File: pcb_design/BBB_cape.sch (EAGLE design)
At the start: 4 parts

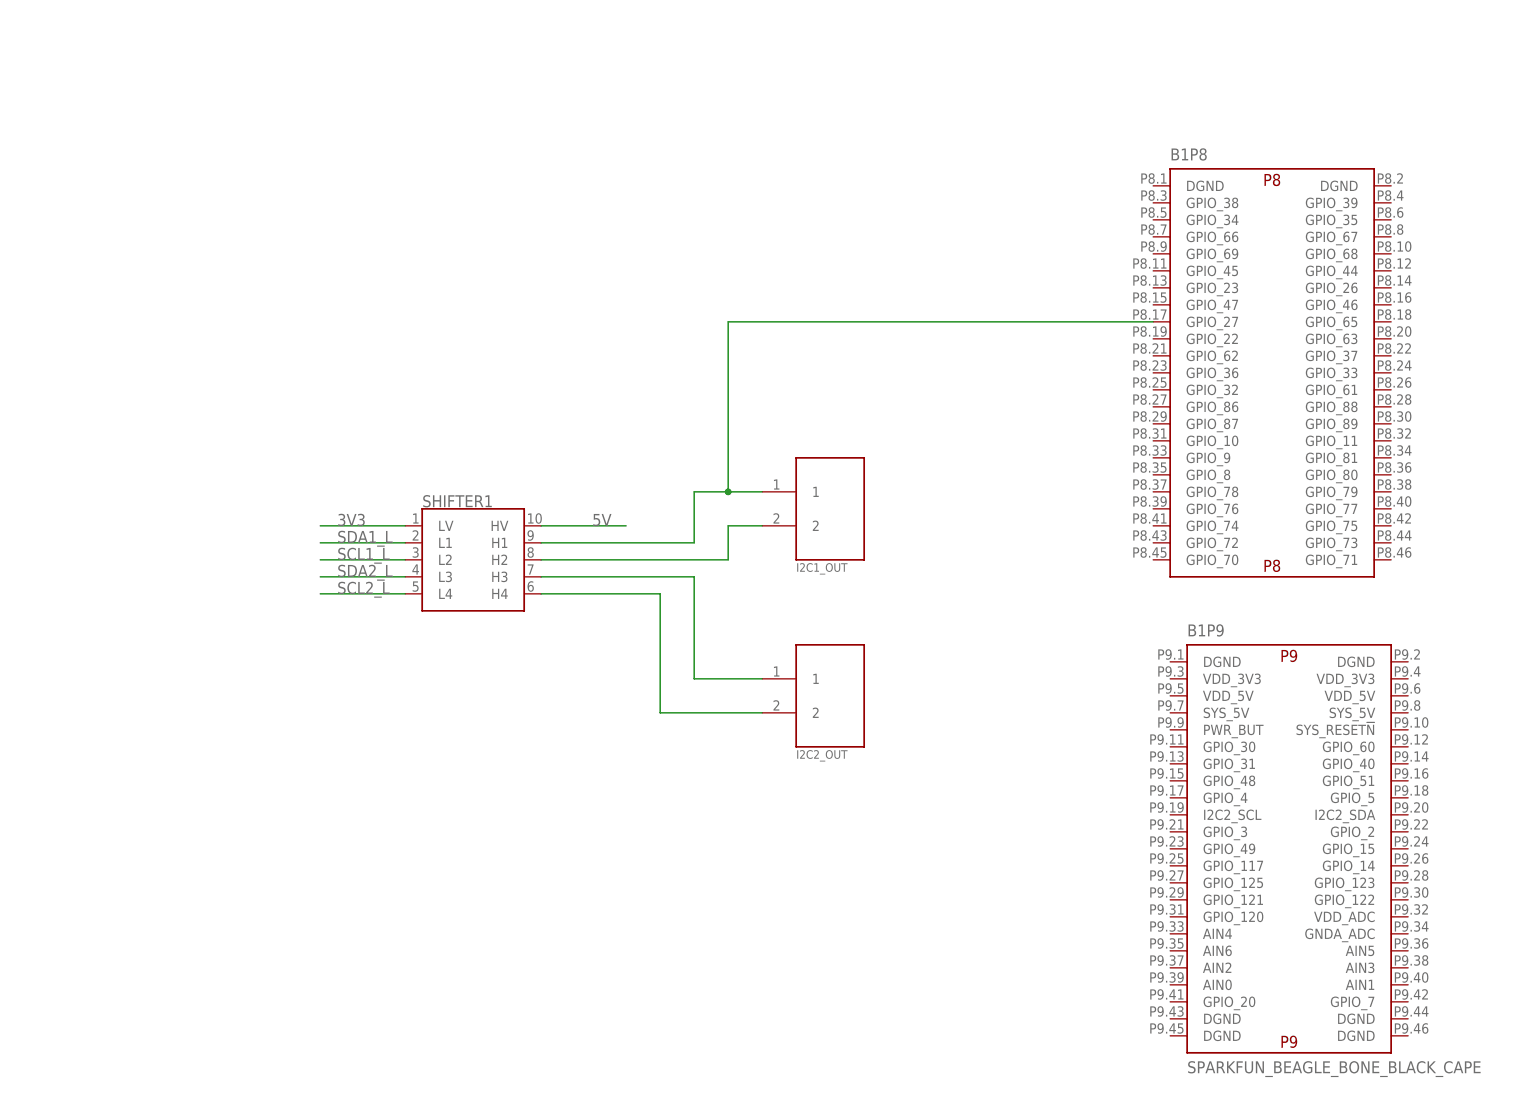
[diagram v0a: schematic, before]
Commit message: added v6 with better connectors and some small drill changes
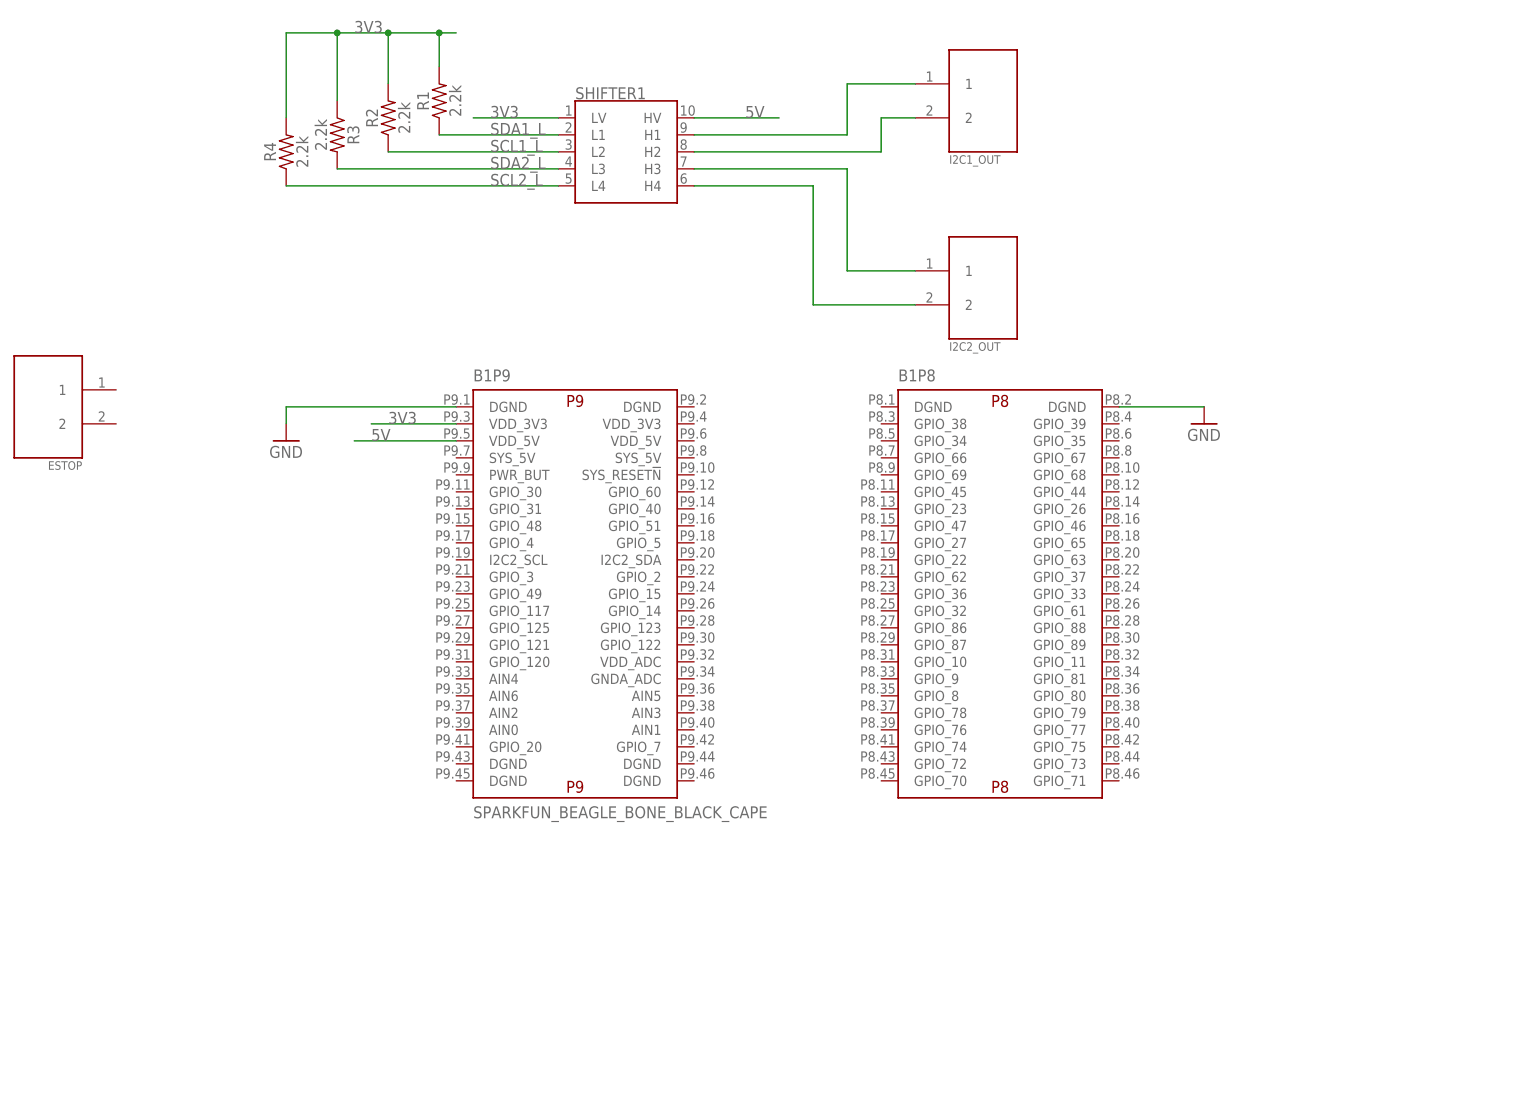
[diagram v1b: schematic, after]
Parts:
- added ESTOP: PHOENIX_CONNECTOR_1778625, byu_pressure_control:PHOENIX_CONNECTOR_1778625
- added R1, R2, R3, R4: 2.2k, SparkFun-Resistors:1KOHM-HORIZ_KIT-1/4W-5%
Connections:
- new net GND: B1P8.DGND@2, B1P9.DGND@1
- net 3V3: now also B1P9.VDD_3V3@1, R1.2, R2.2, R3.1, R4.2
- net 5V: now also B1P9.VDD_5V@1
- net N$1: no longer B1P8.GPIO_27
- net SCL1_L: now also R2.1
- net SCL2_L: now also R4.1
- net SDA1_L: now also R1.1
- net SDA2_L: now also R3.2
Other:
- moved on the sheet: B1P8, B1P9, I2C1_OUT, I2C2_OUT, SHIFTER1

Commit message: removed old files and updated with CAM files for both pcbs.
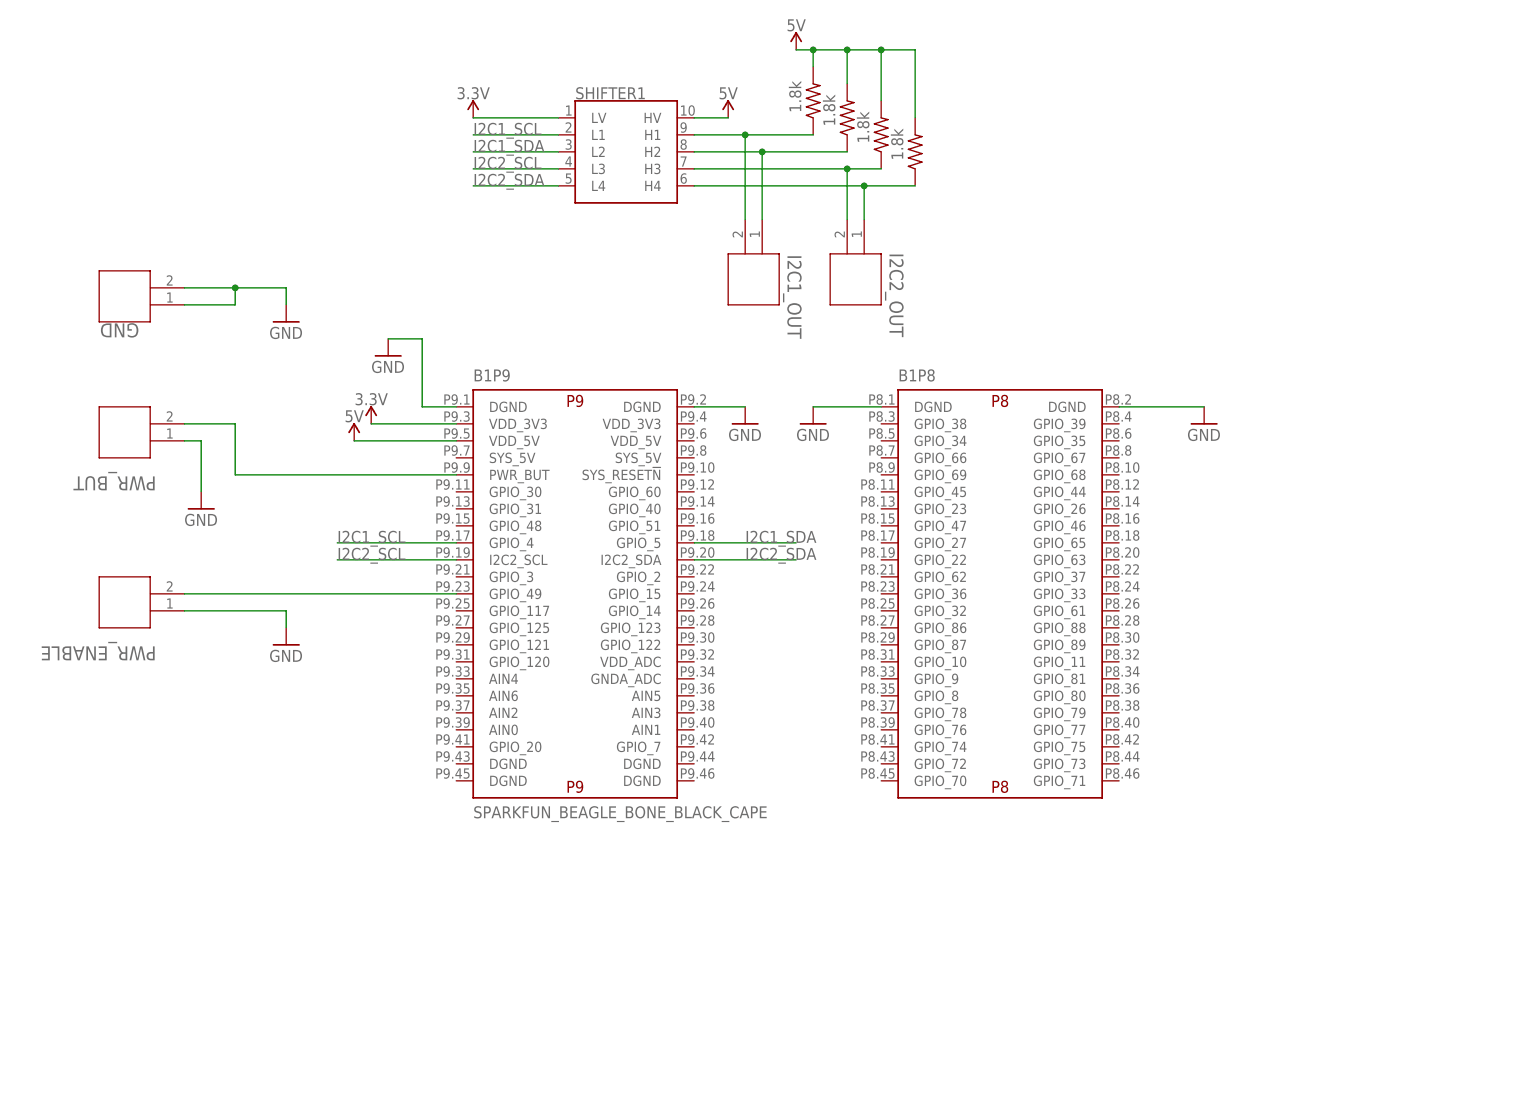
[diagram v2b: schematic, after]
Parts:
- removed ESTOP: PHOENIX_CONNECTOR_1778625, byu_pressure_control:PHOENIX_CONNECTOR_1778625
- added GND, PWR_BUT, PWR_ENABLE: PHOENIX_CONTACT_1758018, byu_pressure_control:PHOENIX_CONTACT_1758018
- I2C1_OUT, I2C2_OUT: value PHOENIX_CONNECTOR_1778625 -> PHOENIX_CONTACT_1758018; device byu_pressure_control:PHOENIX_CONNECTOR_1778625 -> byu_pressure_control:PHOENIX_CONTACT_1758018
- R1, R2, R3, R4: value 2.2k -> 1.8k; device SparkFun-Resistors:1KOHM-HORIZ_KIT-1/4W-5% -> rcl:R-US_0204/7
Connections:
- removed net 3V3: B1P9.VDD_3V3@1, R1.2, R2.2, R3.1, R4.2, SHIFTER1.LV
- removed net SCL1_L: R2.1, SHIFTER1.L2
- removed net SCL2_L: R4.1, SHIFTER1.L4
- removed net SDA1_L: R1.1, SHIFTER1.L1
- removed net SDA2_L: R3.2, SHIFTER1.L3
- new net 3.3V: B1P9.VDD_3V3@1, SHIFTER1.LV
- new net I2C1_SCL: B1P9.GPIO_4, SHIFTER1.L1
- new net I2C1_SDA: B1P9.GPIO_5, SHIFTER1.L2
- new net I2C2_SCL: B1P9.I2C2_SCL, SHIFTER1.L3
- new net I2C2_SDA: B1P9.I2C2_SDA, SHIFTER1.L4
- new net N$5: B1P9.GPIO_49, PWR_ENABLE.2
- new net N$6: B1P9.PWR_BUT, PWR_BUT.2
- net 5V: now also R1.2, R2.2, R3.2, R4.2
- net GND: now also B1P8.DGND@1, B1P9.DGND@2, GND.1, GND.2, PWR_BUT.1, PWR_ENABLE.1
- net N$1: now also I2C1_OUT.2, R1.1; no longer I2C1_OUT.1
- net N$2: now also I2C1_OUT.1, R2.1; no longer I2C1_OUT.2
- net N$3: now also I2C2_OUT.2, R3.1; no longer I2C2_OUT.1
- net N$4: now also I2C2_OUT.1, R4.1; no longer I2C2_OUT.2

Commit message: updated files and cams
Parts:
- R1, R2, R3, R4: value 1.8k -> 2.2k
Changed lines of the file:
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@@
 <part name="GND4" library="supply1" library_urn="urn:adsk.eagle:library:371" deviceset="GND" device=""/>
 <part name="GND5" library="supply1" library_urn="urn:adsk.eagle:library:371" deviceset="GND" device=""/>
-<part name="R1" library="rcl" library_urn="urn:adsk.eagle:library:334" deviceset="R-US_" device="0204/7" package3d_urn="urn:adsk.eagle:package:23498/2" value="1.8k"/>
-<part name="R3" library="rcl" library_urn="urn:adsk.eagle:library:334" deviceset="R-US_" device="0204/7" package3d_urn="urn:adsk.eagle:package:23498/2" value="1.8k"/>
-<part name="R2" library="rcl" library_urn="urn:adsk.eagle:library:334" deviceset="R-US_" device="0204/7" package3d_urn="urn:adsk.eagle:package:23498/2" value="1.8k"/>
-<part name="R4" library="rcl" library_urn="urn:adsk.eagle:library:334" deviceset="R-US_" device="0204/7" package3d_urn="urn:adsk.eagle:package:23498/2" value="1.8k"/>
+<part name="R1" library="rcl" library_urn="urn:adsk.eagle:library:334" deviceset="R-US_" device="0204/7" package3d_urn="urn:adsk.eagle:package:23498/2" value="2.2k"/>
+<part name="R3" library="rcl" library_urn="urn:adsk.eagle:library:334" deviceset="R-US_" device="0204/7" package3d_urn="urn:adsk.eagle:package:23498/2" value="2.2k"/>
+<part name="R2" library="rcl" library_urn="urn:adsk.eagle:library:334" deviceset="R-US_" device="0204/7" package3d_urn="urn:adsk.eagle:package:23498/2" value="2.2k"/>
+<part name="R4" library="rcl" library_urn="urn:adsk.eagle:library:334" deviceset="R-US_" device="0204/7" package3d_urn="urn:adsk.eagle:package:23498/2" value="2.2k"/>
 <part name="GND" library="byu_pressure_control" library_urn="urn:adsk.eagle:library:26800355" deviceset="PHOENIX_CONTACT_1758018" device="" package3d_urn="urn:adsk.eagle:package:28556303/3"/>
 <part name="GND6" library="supply1" library_urn="urn:adsk.eagle:library:371" deviceset="GND" device=""/>
